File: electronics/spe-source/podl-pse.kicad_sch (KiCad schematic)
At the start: 21 parts, among them Q1 2N7002P, Q2 DMP6350SQ, U1 TLV6700, U3 NSI50010YT1G, U5 S-1212-7V

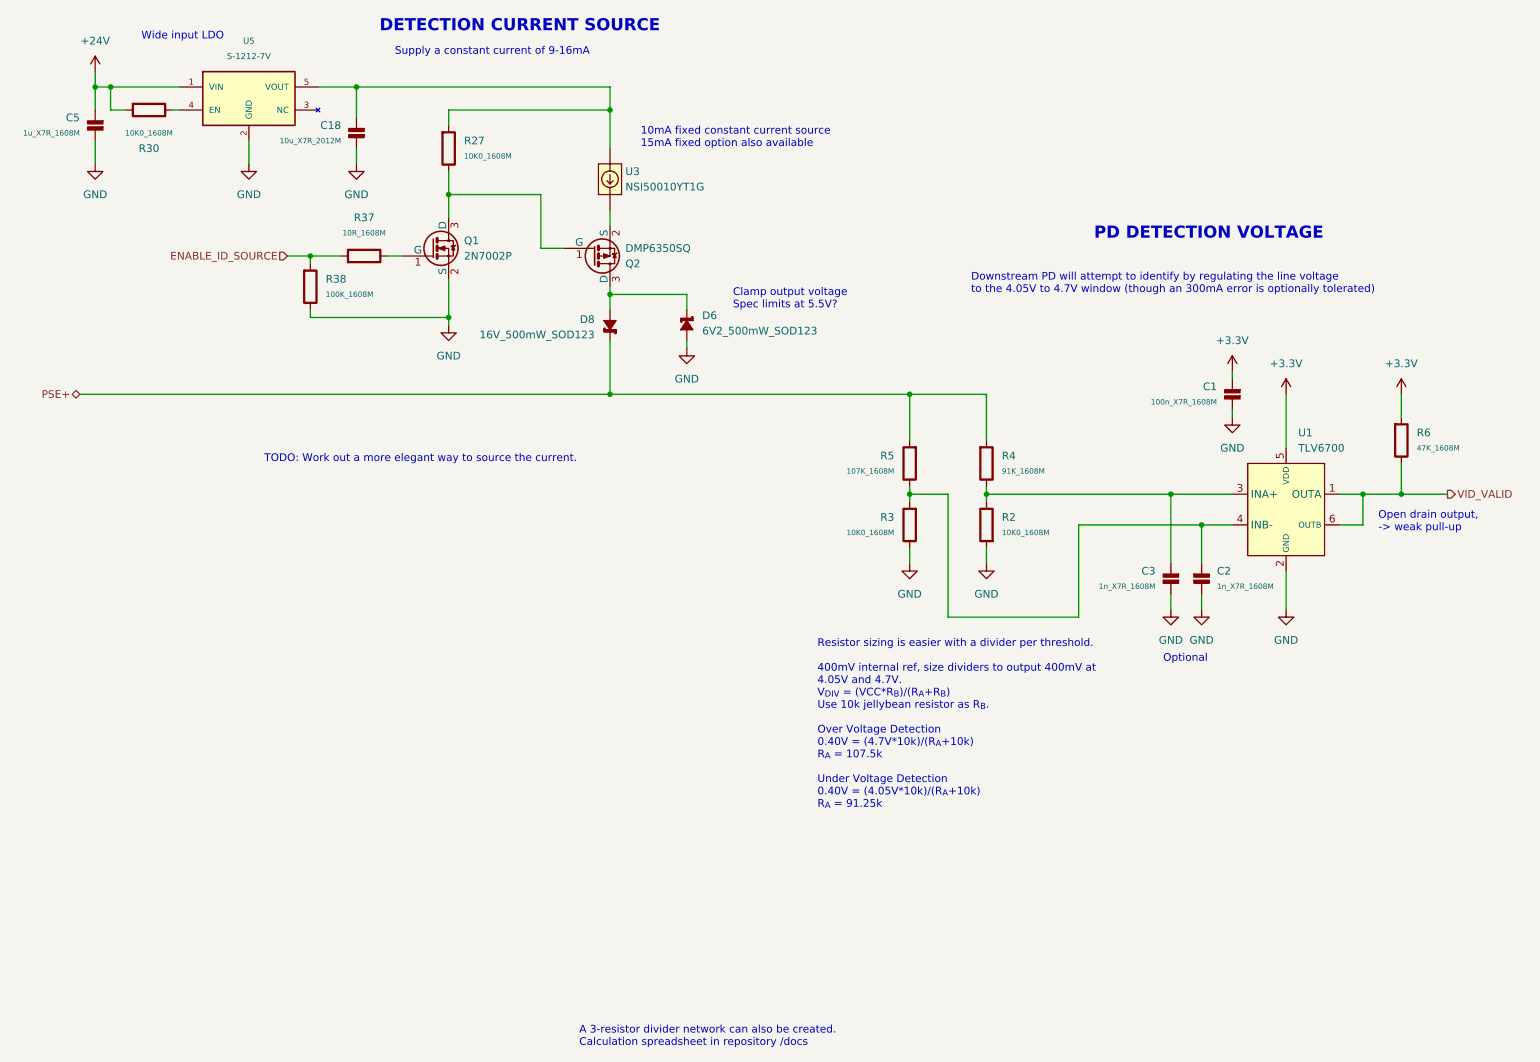
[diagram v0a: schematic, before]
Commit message: PSE part placement, partial routing
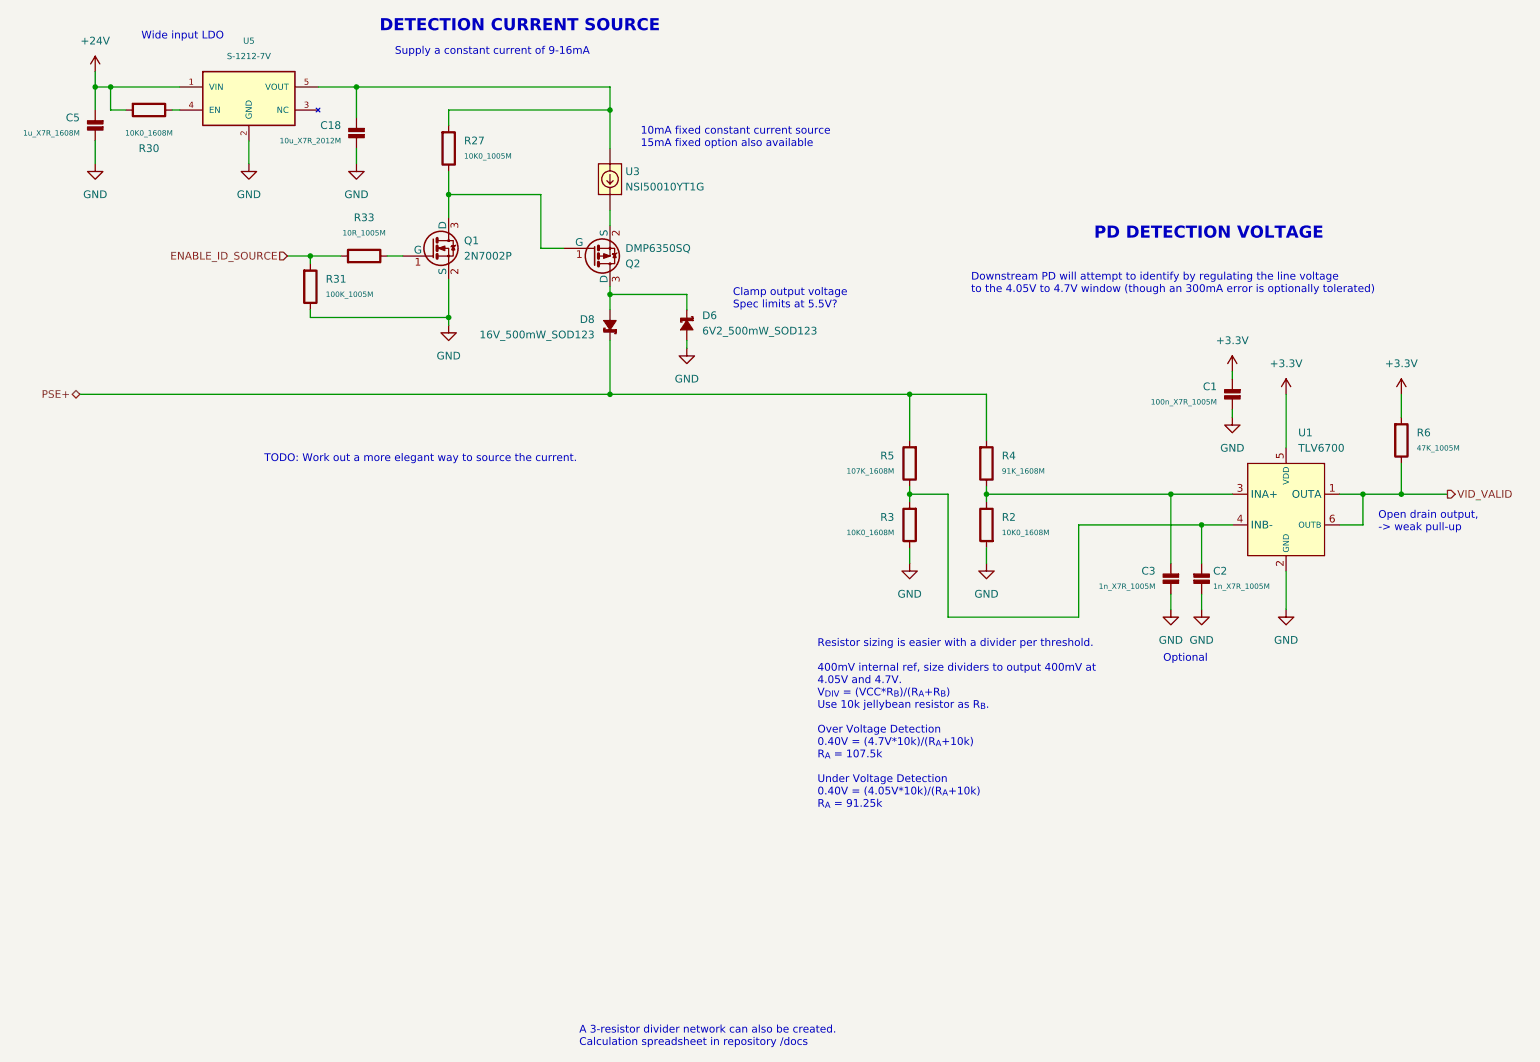
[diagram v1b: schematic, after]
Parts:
- removed C1: 100n_X7R_1608M, Applidyne_Capacitor:CAPC1608X90N, symbol appli_capacitor:100n_X7R_1608M
- removed C2, C3: 1n_X7R_1608M, Applidyne_Capacitor:CAPC1608X90N, symbol appli_capacitor:1n_X7R_1608M
- removed R27: 10K0_1608M, Applidyne_Resistor:RESC1608X50N, symbol appli_resistor:10K0_1608M
- removed R37: 10R_1608M, Applidyne_Resistor:RESC1608X50N, symbol appli_resistor:10R_1608M
- removed R38: 100K_1608M, Applidyne_Resistor:RESC1608X50N, symbol appli_resistor:100K_1608M
- removed R6: 47K_1608M, Applidyne_Resistor:RESC1608X50N, symbol appli_resistor:47K_1608M
- added C1: 100n_X7R_1005M, Applidyne_Capacitor:CAPC1005X60N, symbol appli_capacitor:100n_X7R_1005M
- added C2, C3: 1n_X7R_1005M, Applidyne_Capacitor:CAPC1005X60N, symbol appli_capacitor:1n_X7R_1005M
- added R27: 10K0_1005M, Applidyne_Resistor:RESC1005X40N, symbol appli_resistor:10K0_1005M
- added R31: 100K_1005M, Applidyne_Resistor:RESC1005X40N, symbol appli_resistor:100K_1005M
- added R33: 10R_1005M, Applidyne_Resistor:RESC1005X40N, symbol appli_resistor:10R_1005M
- added R6: 47K_1005M, Applidyne_Resistor:RESC1005X40N, symbol appli_resistor:47K_1005M
- C5: footprint CAPC1608* -> Applidyne_Capacitor:CAPC1608X90N
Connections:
- net +3.3V: now also C1.1, R6.1
- net ENABLE_ID_SOURCE: now also R31.1, R33.1
- net GND: now also C1.2, C2.2, C3.2, R31.2
- net VID_VALID: now also R6.2
- net at Q1.1 (G): now also R33.2
- net at Q1.3 (D), Q2.1 (G): now also R27.2
- net at Q2.2 (S): now also U3.C; no longer U3.1 (C)
- net at R2.2, R4.2, U1.3 (INA+): now also C3.1
- net at R3.1, R5.2, U1.4 (INB-): now also C2.1
- net at C18.1, U5.5 (VOUT): now also U3.A, R27.1; no longer U3.2 (A)

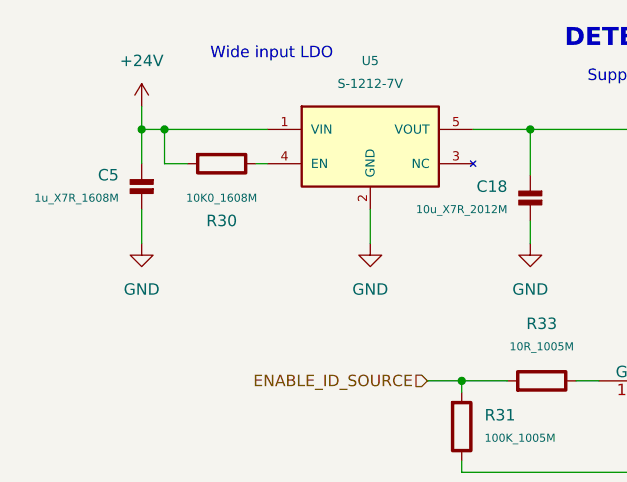
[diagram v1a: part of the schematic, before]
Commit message: PSE routing spaghetti complete
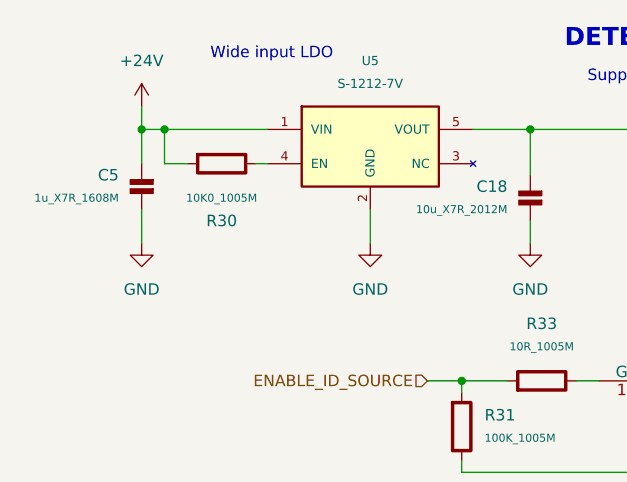
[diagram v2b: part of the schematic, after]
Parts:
- removed R30: 10K0_1608M, Applidyne_Resistor:RESC1608X50N, symbol appli_resistor:10K0_1608M
- added R30: 10K0_1005M, Applidyne_Resistor:RESC1005X40N, symbol appli_resistor:10K0_1005M
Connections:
- net +24V: now also R30.1
- net at U5.4 (EN): now also R30.2
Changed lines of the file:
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@@
+    )
+  )
+  (symbol (lib_id "appli_resistor:10K0_1005M") (at 48.26 38.1 90) (mirror x) (unit 1)
+    (in_bom yes) (on_board yes) (dnp no)
+    (property "Reference" "R30" (at 52.07 44.45 90)
+      (effects (font (size 1.27 1.27)))
+    )
+    (property "Value" "10K0_1005M" (at 52.07 41.91 90)
+      (effects (font (size 0.889 0.889)))
+    )
+    (property "Footprint" "Applidyne_Resistor:RESC1005X40N" (at 52.07 40.894 90)
+      (effects (font (size 0.508 0.508)) hide)
+    )
+    (property "Datasheet" "http://www.farnell.com/datasheets/2111203.pdf" (at 52.07 41.529 90)
+      (effects (font (size 0.508 0.508)) hide)
+    )
+    (property "manf" "VISHAY" (at 52.07 42.799 90)
+      (effects (font (size 0.508 0.508)) hide)
+    )
+    (property "manf#" "CRCW040210K0FKED" (at 52.07 43.434 90)
+      (effects (font (size 0.508 0.508)) hide)
+    )
+    (property "Supplier" "Element14" (at 52.07 44.069 90)
+      (effects (font (size 0.508 0.508)) hide)
+    )
+    (property "Supplier Part No" "1469669" (at 52.07 44.704 90)
+      (effects (font (size 0.508 0.508)) hide)
+    )
+    (property "Supplier URL" "http://au.element14.com/vishay/crcw040210k0fked/res-thick-film-10k-1-0-063w-0402/dp/1469669" (at 52.07 45.339 90)
+      (effects (font (size 0.508 0.508)) hide)
+    )
+    (property "Supplier Price" "0.009" (at 52.07 45.974 90)
+      (effects (font (size 0.508 0.508)) hide)
+    )
+    (property "Supplier Price Break" "10" (at 52.07 46.609 90)
+      (effects (font (size 0.508 0.508)) hide)
+    )
+    (pin "1")
+    (pin "2")
+    (instances
+      (project "spe-source"
+        (path "/f0a501c7-1ad1-4c59-9255-3d6aa4545d8b/d94cf2f8-a9f8-40b0-8c4c-eef4bcbb8aa0"
+          (reference "R30") (unit 1)
+        )
+      )
     )
   )
@@
         )
       )
-    )
-  )
-  (symbol (lib_id "appli_resistor:10K0_1608M") (at 48.26 38.1 90) (mirror x) (unit 1)
-    (in_bom yes) (on_board yes) (dnp no)
-    (property "Reference" "R30" (at 52.07 44.45 90)
-      (effects (font (size 1.27 1.27)))
-    )
-    (property "Value" "10K0_1608M" (at 52.07 41.91 90)
-      (effects (font (size 0.889 0.889)))
-    )
-    (property "Footprint" "Applidyne_Resistor:RESC1608X50N" (at 52.07 40.894 90)
-      (effects (font (size 0.508 0.508)) hide)
-    )
-    (property "Datasheet" "http://www.farnell.com/datasheets/1723233.pdf" (at 52.07 41.529 90)
-      (effects (font (size 0.508 0.508)) hide)
-    )
-    (property "manf" "TE CONNECTIVITY" (at 52.07 42.799 90)
-      (effects (font (size 0.508 0.508)) hide)
-    )
-    (property "manf#" "CRGH0603F10K" (at 52.07 43.434 90)
-      (effects (font (size 0.508 0.508)) hide)
-    )
-    (property "Supplier" "Element14" (at 52.07 44.069 90)
-      (effects (font (size 0.508 0.508)) hide)
-    )
-    (property "Supplier Part No" "2332016" (at 52.07 44.704 90)
-      (effects (font (size 0.508 0.508)) hide)
-    )
-    (property "Supplier URL" "http://au.element14.com/te-connectivity/crgh0603f10k/resistor-power-10k-0-2w-1-0603/dp/2332016" (at 52.07 45.339 90)
-      (effects (font (size 0.508 0.508)) hide)
-    )
-    (property "Supplier Price" "0.02" (at 52.07 45.974 90)
-      (effects (font (size 0.508 0.508)) hide)
-    )
-    (property "Supplier Price Break" "10" (at 52.07 46.609 90)
-      (effects (font (size 0.508 0.508)) hide)
-    )
-    (pin "1")
-    (pin "2")
-    (instances
-      (project "spe-source"
-        (path "/f0a501c7-1ad1-4c59-9255-3d6aa4545d8b/d94cf2f8-a9f8-40b0-8c4c-eef4bcbb8aa0"
-          (reference "R30") (unit 1)
-        )
-      )

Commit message: Minor tweaks to test sketches
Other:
- note added: "Downstream PD will attempt to identify by regulating the line voltage to the 4.05V to 4.7V window (though an 300mV error is optionally tolerated)"
- note removed: "Downstream PD will attempt to identify by regulating the line voltage to the 4.05V to 4.7V window (though an 300mA error is optionally tolerated)"
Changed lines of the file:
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@@
     (effects (font (size 1.27 1.27)) (justify left bottom))
   )
-  (text "Downstream PD will attempt to identify by regulating the line voltage\nto the 4.05V to 4.7V window (though an 300mA error is optionally tolerated)"
+  (text "Downstream PD will attempt to identify by regulating the line voltage\nto the 4.05V to 4.7V window (though an 300mV error is optionally tolerated)"
     (at 187.96 68.58 0)
     (effects (font (size 1.27 1.27)) (justify left bottom))

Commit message: Random uncommitted KiCAD tweaks
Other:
- note added: "TODO: Replace with higher voltage rated diode"
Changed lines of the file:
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@@
     (effects (font (size 2 2) (thickness 0.6) bold) (justify left bottom))
+  )
+  (text "TODO: Replace with higher \nvoltage rated diode" (at 107.315 83.185 0)
+    (effects (font (size 1.27 1.27)) (justify left bottom))
   )
   (text "10mA fixed constant current source\n15mA fixed option also available"
